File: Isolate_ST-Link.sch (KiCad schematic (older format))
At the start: 17 parts

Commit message: スピードの切り替えにジャンパを追加
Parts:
- added C? (x2): C, symbol C
- added J? (x2): GS3, Connectors:GS3, symbol GS3
- added R?: R, symbol R
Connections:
- net GND: now also J?.3 (G3)
- net GNDPWR: now also C?.1, C?.2, J?.3 (G3)
- net at J?.1 (VBUS): now also U?.1 (V_BUS1), C?.1
- net at U?.12 (PIN): now also R?.2
- net at U?.13 (SPD): now also J?.2 (G2)
- net at U?.14 (VDD2): now also J?.1 (G1), R?.1
- net at U?.3 (VDD1): now also C?.2, J?.1 (G1)
- net at U?.5 (SPU): now also J?.2 (G2)
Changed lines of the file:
@@
 $EndComp
 Wire Wire Line
-	8200 4550 9250 4550
-Wire Wire Line
-	8700 4350 8700 4650
-Wire Wire Line
-	8200 4450 9250 4450
-Wire Wire Line
-	8950 4350 8950 4650
+	8200 4550 8700 4550
+Wire Wire Line
+	8700 4550 9250 4550
+Wire Wire Line
+	8700 4350 8700 4550
+Wire Wire Line
+	8700 4550 8700 4650
+Wire Wire Line
+	8200 4450 8950 4450
+Wire Wire Line
+	8950 4450 9250 4450
+Wire Wire Line
+	8950 4350 8950 4450
+Wire Wire Line
+	8950 4450 8950 4650
 $Comp
 L GND #PWR?
@@
 $EndComp
 Wire Wire Line
-	2000 4650 2000 4850
+	2000 4650 2000 4700
+Wire Wire Line
+	2000 4700 2000 4850
 Wire Wire Line
 	1900 4650 1900 4700
@@
 $EndComp
 Wire Wire Line
-	6900 3200 7100 3200
+	6900 3200 7000 3200
+Wire Wire Line
+	7000 3200 7100 3200
 Wire Wire Line
 	6900 2900 7000 2900
@@
 	5350 3750 5450 3750
 Wire Wire Line
-	5450 3750 5450 4400
+	5450 3750 5450 4350
+Wire Wire Line
+	5450 4350 5450 4400
 Wire Wire Line
 	5350 4350 5450 4350
@@
 $EndComp
 Wire Wire Line
-	4350 4400 4350 3750
+	4350 3750 4350 4350
+Wire Wire Line
+	4350 4350 4350 4400
+Wire Wire Line
+	4000 3750 4350 3750
 Wire Wire Line
 	4350 3750 4450 3750
@@
 Wire Wire Line
 	4150 4350 2300 4350
+$Comp
+L C C?
+U 1 1 59487B46
+P 3800 3800
+F 0 "C?" H 3825 3900 50  0000 L CNN
+F 1 "C" H 3825 3700 50  0000 L CNN
+F 2 "" H 3838 3650 50  0001 C CNN
+F 3 "" H 3800 3800 50  0001 C CNN
+	1    3800 3800
+	1    0    0    -1
+$EndComp
+Wire Wire Line
+	4450 3850 4000 3850
+Wire Wire Line
+	4000 3950 4000 3850
+Wire Wire Line
+	3650 3950 3800 3950
+Wire Wire Line
+	3800 3950 4000 3950
+Wire Wire Line
+	4000 3750 4000 3650
+Wire Wire Line
+	4000 3650 3800 3650
+Connection ~ 4350 3750
+$Comp
+L C C?
+U 1 1 59488111
+P 3800 3500
+F 0 "C?" H 3825 3600 50  0000 L CNN
+F 1 "C" H 3825 3400 50  0000 L CNN
+F 2 "" H 3838 3350 50  0001 C CNN
+F 3 "" H 3800 3500 50  0001 C CNN
+	1    3800 3500
+	1    0    0    -1
+$EndComp
+Wire Wire Line
+	4450 3650 4200 3650
+Wire Wire Line
+	4200 3350 4200 3650
+Wire Wire Line
+	2700 3350 3800 3350
+Wire Wire Line
+	3800 3350 4200 3350
+Wire Wire Line
+	2300 4050 2700 4050
+Wire Wire Line
+	2700 4050 2700 3350
+Connection ~ 3800 3350
+$Comp
+L GS3 J?
+U 1 1 594888C1
+P 3500 4050
+F 0 "J?" H 3550 4250 50  0000 C CNN
+F 1 "GS3" H 3550 3851 50  0000 C CNN
+F 2 "Connectors:GS3" V 3588 3976 50  0001 C CNN
+F 3 "" H 3500 4050 50  0001 C CNN
+	1    3500 4050
+	1    0    0    -1
+$EndComp
+$Comp
+L GS3 J?
+U 1 1 5948896E
+P 6250 3950
+F 0 "J?" H 6300 4150 50  0000 C CNN
+F 1 "GS3" H 6300 3751 50  0000 C CNN
+F 2 "Connectors:GS3" V 6338 3876 50  0001 C CNN
+F 3 "" H 6250 3950 50  0001 C CNN
+	1    6250 3950
+	-1   0    0    -1
+$EndComp
+Wire Wire Line
+	4450 4050 3650 4050
+$Comp
+L GNDPWR #PWR?
+U 1 1 59488AB0
+P 3300 4450
+F 0 "#PWR?" H 3300 4250 50  0001 C CNN
+F 1 "GNDPWR" H 3300 4320 50  0000 C CNN
+F 2 "" H 3300 4400 50  0001 C CNN
+F 3 "" H 3300 4400 50  0001 C CNN
+	1    3300 4450
+	1    0    0    -1
+$EndComp
+Wire Wire Line
+	3350 4150 3300 4150
+Wire Wire Line
+	3300 4150 3300 4450
+Wire Wire Line
+	3350 3950 3300 3950
+Wire Wire Line
+	3300 3950 3300 3750
+Wire Wire Line
+	3300 3750 3650 3750
+Wire Wire Line
+	3650 3750 3650 3950
+Connection ~ 3800 3950
+Wire Wire Line
+	5350 3950 6100 3950
+$Comp
+L GND #PWR?
+U 1 1 5948984E
+P 6400 4400
+F 0 "#PWR?" H 6400 4150 50  0001 C CNN
+F 1 "GND" H 6400 4250 50  0000 C CNN
+F 2 "" H 6400 4400 50  0001 C CNN
+F 3 "" H 6400 4400 50  0001 C CNN
+	1    6400 4400
+	1    0    0    -1
+$EndComp
+Wire Wire Line
+	6400 4400 6400 4050
+Wire Wire Line
+	6400 4050 6400 4050
+Wire Wire Line
+	5350 3850 5950 3850
+Wire Wire Line
+	5950 3850 5950 3850
+Wire Wire Line
+	5950 3850 5950 3700
+Wire Wire Line
+	5950 3700 6400 3700
+Wire Wire Line
+	6400 3700 6400 3850
+Wire Wire Line
+	6400 3850 6400 3850
+$Comp
+L R R?
+U 1 1 59489C26
+P 5700 4050
+F 0 "R?" V 5780 4050 50  0000 C CNN
+F 1 "R" V 5700 4050 50  0000 C CNN
+F 2 "" V 5630 4050 50  0001 C CNN
+F 3 "" H 5700 4050 50  0001 C CNN
+	1    5700 4050
+	0    1    1    0
+$EndComp
+Wire Wire Line
+	5350 4050 5550 4050
+Wire Wire Line
+	5850 4050 5950 4050
+Wire Wire Line
+	5950 4050 5950 3850
+Connection ~ 5950 3850
 $EndSCHEMATC

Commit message: 簡素にした
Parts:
- removed J? (x2): GS3, Connectors:GS3, symbol GS3
- removed R?: R, symbol R
- added C? (x2): C, symbol C
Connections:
- net GND: now also C?.1, C?.2
- net at C?.2, U?.3 (VDD1): now also U?.4 (PDEN), U?.5 (SPU)
- net at U?.14 (VDD2): now also U?.12 (PIN), U?.13 (SPD), C?.2
- net at U?.16 (VBUS2): now also C?.1
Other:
- moved on the sheet: C?
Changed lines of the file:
@@
 $EndComp
 Wire Wire Line
-	8200 4550 8700 4550
-Wire Wire Line
-	8700 4550 9250 4550
-Wire Wire Line
-	8700 4350 8700 4550
-Wire Wire Line
-	8700 4550 8700 4650
-Wire Wire Line
-	8200 4450 8950 4450
-Wire Wire Line
-	8950 4450 9250 4450
-Wire Wire Line
-	8950 4350 8950 4450
-Wire Wire Line
-	8950 4450 8950 4650
+	8200 4550 9250 4550
+Wire Wire Line
+	8700 4350 8700 4650
+Wire Wire Line
+	8200 4450 9250 4450
+Wire Wire Line
+	8950 4350 8950 4650
 $Comp
 L GND #PWR?
@@
 $EndComp
 Wire Wire Line
-	2000 4650 2000 4700
-Wire Wire Line
-	2000 4700 2000 4850
+	2000 4650 2000 4850
 Wire Wire Line
 	1900 4650 1900 4700
@@
 $EndComp
 Wire Wire Line
-	6900 3200 7000 3200
-Wire Wire Line
-	7000 3200 7100 3200
+	6900 3200 7100 3200
 Wire Wire Line
 	6900 2900 7000 2900
@@
 L GND #PWR?
 U 1 1 5949B992
-P 5450 4400
-F 0 "#PWR?" H 5450 4150 50  0001 C CNN
-F 1 "GND" H 5450 4250 50  0000 C CNN
-F 2 "" H 5450 4400 50  0001 C CNN
-F 3 "" H 5450 4400 50  0001 C CNN
-	1    5450 4400
-	1    0    0    -1
-$EndComp
-Wire Wire Line
-	5350 3750 5450 3750
-Wire Wire Line
-	5450 3750 5450 4350
-Wire Wire Line
-	5450 4350 5450 4400
-Wire Wire Line
-	5350 4350 5450 4350
-Connection ~ 5450 4350
+P 5800 4400
+F 0 "#PWR?" H 5800 4150 50  0001 C CNN
+F 1 "GND" H 5800 4250 50  0000 C CNN
+F 2 "" H 5800 4400 50  0001 C CNN
+F 3 "" H 5800 4400 50  0001 C CNN
+	1    5800 4400
+	1    0    0    -1
+$EndComp
+Wire Wire Line
+	5800 3750 5800 4400
+Wire Wire Line
+	5350 4350 6000 4350
+Connection ~ 5800 4350
 $Comp
 L R R?
@@
 L GNDPWR #PWR?
 U 1 1 5949CF3F
-P 4350 4400
-F 0 "#PWR?" H 4350 4200 50  0001 C CNN
-F 1 "GNDPWR" H 4350 4270 50  0000 C CNN
-F 2 "" H 4350 4350 50  0001 C CNN
-F 3 "" H 4350 4350 50  0001 C CNN
-	1    4350 4400
-	1    0    0    -1
-$EndComp
-Wire Wire Line
-	4350 3750 4350 4350
-Wire Wire Line
-	4350 4350 4350 4400
-Wire Wire Line
-	4000 3750 4350 3750
-Wire Wire Line
-	4350 3750 4450 3750
-Wire Wire Line
-	4450 4350 4350 4350
-Connection ~ 4350 4350
+P 4000 4400
+F 0 "#PWR?" H 4000 4200 50  0001 C CNN
+F 1 "GNDPWR" H 4000 4270 50  0000 C CNN
+F 2 "" H 4000 4350 50  0001 C CNN
+F 3 "" H 4000 4350 50  0001 C CNN
+	1    4000 4400
+	1    0    0    -1
+$EndComp
 Wire Wire Line
 	4450 4250 2300 4250
 Wire Wire Line
-	4450 4150 4150 4150
-Wire Wire Line
-	4150 4150 4150 4350
-Wire Wire Line
-	4150 4350 2300 4350
+	4450 4150 3200 4150
+Wire Wire Line
+	3200 4150 3200 4350
+Wire Wire Line
+	3200 4350 2300 4350
 $Comp
 L C C?
 U 1 1 59487B46
-P 3800 3800
-F 0 "C?" H 3825 3900 50  0000 L CNN
-F 1 "C" H 3825 3700 50  0000 L CNN
-F 2 "" H 3838 3650 50  0001 C CNN
-F 3 "" H 3800 3800 50  0001 C CNN
-	1    3800 3800
-	1    0    0    -1
-$EndComp
-Wire Wire Line
-	4450 3850 4000 3850
-Wire Wire Line
-	4000 3950 4000 3850
-Wire Wire Line
-	3650 3950 3800 3950
-Wire Wire Line
-	3800 3950 4000 3950
-Wire Wire Line
-	4000 3750 4000 3650
-Wire Wire Line
-	4000 3650 3800 3650
-Connection ~ 4350 3750
+P 4200 3900
+F 0 "C?" H 4225 4000 50  0000 L CNN
+F 1 "C" H 4225 3800 50  0000 L CNN
+F 2 "" H 4238 3750 50  0001 C CNN
+F 3 "" H 4200 3900 50  0001 C CNN
+	1    4200 3900
+	1    0    0    -1
+$EndComp
+Wire Wire Line
+	4450 3850 4400 3850
+Wire Wire Line
+	4400 3850 4400 4050
+Wire Wire Line
+	4400 3950 4450 3950
 $Comp
 L C C?
 U 1 1 59488111
-P 3800 3500
-F 0 "C?" H 3825 3600 50  0000 L CNN
-F 1 "C" H 3825 3400 50  0000 L CNN
-F 2 "" H 3838 3350 50  0001 C CNN
-F 3 "" H 3800 3500 50  0001 C CNN
-	1    3800 3500
-	1    0    0    -1
-$EndComp
-Wire Wire Line
-	4450 3650 4200 3650
-Wire Wire Line
-	4200 3350 4200 3650
-Wire Wire Line
-	2700 3350 3800 3350
-Wire Wire Line
-	3800 3350 4200 3350
+P 3800 3900
+F 0 "C?" H 3825 4000 50  0000 L CNN
+F 1 "C" H 3825 3800 50  0000 L CNN
+F 2 "" H 3838 3750 50  0001 C CNN
+F 3 "" H 3800 3900 50  0001 C CNN
+	1    3800 3900
+	1    0    0    -1
+$EndComp
+Wire Wire Line
+	2700 3650 4450 3650
 Wire Wire Line
 	2300 4050 2700 4050
 Wire Wire Line
-	2700 4050 2700 3350
-Connection ~ 3800 3350
-$Comp
-L GS3 J?
-U 1 1 594888C1
-P 3500 4050
-F 0 "J?" H 3550 4250 50  0000 C CNN
-F 1 "GS3" H 3550 3851 50  0000 C CNN
-F 2 "Connectors:GS3" V 3588 3976 50  0001 C CNN
-F 3 "" H 3500 4050 50  0001 C CNN
-	1    3500 4050
-	1    0    0    -1
-$EndComp
-$Comp
-L GS3 J?
-U 1 1 5948896E
-P 6250 3950
-F 0 "J?" H 6300 4150 50  0000 C CNN
-F 1 "GS3" H 6300 3751 50  0000 C CNN
-F 2 "Connectors:GS3" V 6338 3876 50  0001 C CNN
-F 3 "" H 6250 3950 50  0001 C CNN
-	1    6250 3950
-	-1   0    0    -1
-$EndComp
-Wire Wire Line
-	4450 4050 3650 4050
-$Comp
-L GNDPWR #PWR?
-U 1 1 59488AB0
-P 3300 4450
-F 0 "#PWR?" H 3300 4250 50  0001 C CNN
-F 1 "GNDPWR" H 3300 4320 50  0000 C CNN
-F 2 "" H 3300 4400 50  0001 C CNN
-F 3 "" H 3300 4400 50  0001 C CNN
-	1    3300 4450
-	1    0    0    -1
-$EndComp
-Wire Wire Line
-	3350 4150 3300 4150
-Wire Wire Line
-	3300 4150 3300 4450
-Wire Wire Line
-	3350 3950 3300 3950
-Wire Wire Line
-	3300 3950 3300 3750
-Wire Wire Line
-	3300 3750 3650 3750
-Wire Wire Line
-	3650 3750 3650 3950
-Connection ~ 3800 3950
-Wire Wire Line
-	5350 3950 6100 3950
-$Comp
-L GND #PWR?
-U 1 1 5948984E
-P 6400 4400
-F 0 "#PWR?" H 6400 4150 50  0001 C CNN
-F 1 "GND" H 6400 4250 50  0000 C CNN
-F 2 "" H 6400 4400 50  0001 C CNN
-F 3 "" H 6400 4400 50  0001 C CNN
-	1    6400 4400
-	1    0    0    -1
-$EndComp
-Wire Wire Line
-	6400 4400 6400 4050
-Wire Wire Line
-	6400 4050 6400 4050
-Wire Wire Line
-	5350 3850 5950 3850
-Wire Wire Line
-	5950 3850 5950 3850
-Wire Wire Line
-	5950 3850 5950 3700
-Wire Wire Line
-	5950 3700 6400 3700
-Wire Wire Line
-	6400 3700 6400 3850
-Wire Wire Line
-	6400 3850 6400 3850
-$Comp
-L R R?
-U 1 1 59489C26
-P 5700 4050
-F 0 "R?" V 5780 4050 50  0000 C CNN
-F 1 "R" V 5700 4050 50  0000 C CNN
-F 2 "" V 5630 4050 50  0001 C CNN
-F 3 "" H 5700 4050 50  0001 C CNN
-	1    5700 4050
-	0    1    1    0
-$EndComp
-Wire Wire Line
-	5350 4050 5550 4050
-Wire Wire Line
-	5850 4050 5950 4050
-Wire Wire Line
-	5950 4050 5950 3850
-Connection ~ 5950 3850
+	5350 4050 5600 4050
+Connection ~ 4400 3950
+Wire Wire Line
+	4200 4050 4450 4050
+Connection ~ 4400 4050
+Wire Wire Line
+	4000 3750 4450 3750
+Connection ~ 4200 3750
+Wire Wire Line
+	4000 3750 4000 4400
+Wire Wire Line
+	3800 4350 4450 4350
+Connection ~ 4000 4350
+$Comp
+L C C?
+U 1 1 5949101E
+P 5600 3900
+F 0 "C?" H 5625 4000 50  0000 L CNN
+F 1 "C" H 5625 3800 50  0000 L CNN
+F 2 "" H 5638 3750 50  0001 C CNN
+F 3 "" H 5600 3900 50  0001 C CNN
+	1    5600 3900
+	1    0    0    -1
+$EndComp
+Wire Wire Line
+	5350 3850 5400 3850
+Wire Wire Line
+	5400 3850 5400 4050
+Connection ~ 5400 4050
+Wire Wire Line
+	5350 3950 5400 3950
+Connection ~ 5400 3950
+Wire Wire Line
+	5350 3650 6000 3650
+Wire Wire Line
+	5350 3750 5800 3750
+Connection ~ 5600 3750
+$Comp
+L C C?
+U 1 1 59497D6D
+P 6000 3900
+F 0 "C?" H 6025 4000 50  0000 L CNN
+F 1 "C" H 6025 3800 50  0000 L CNN
+F 2 "" H 6038 3750 50  0001 C CNN
+F 3 "" H 6000 3900 50  0001 C CNN
+	1    6000 3900
+	1    0    0    -1
+$EndComp
+Wire Wire Line
+	6000 3650 6000 3750
+Wire Wire Line
+	6000 4350 6000 4050
+Wire Wire Line
+	2700 4050 2700 3650
+Wire Wire Line
+	3800 4350 3800 4050
+Wire Wire Line
+	3800 3750 3800 3650
+Connection ~ 3800 3650
 $EndSCHEMATC

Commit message: 基板起こした
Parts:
- removed C? (x3): C, symbol C
- removed R? (x2): R, symbol R
- added C1: 47u, Capacitors_SMD:C_1206, symbol C
- added C2, C3, C5: 0.1u, Capacitors_SMD:C_0603, symbol C
- added C6, C7: 1u, Capacitors_SMD:C_0603, symbol C
- added D10, D9: D, Diodes_SMD:D_SOD-123F, symbol D
- added D5, D6, D7, D8: LED, LEDs:LED_0603, symbol LED
- added F1, F2: Fuse, Capacitors_SMD:C_0603, symbol Fuse
- added J4, J5: CONN_01X02, Connectors_JST:JST_EH_S02B-EH_02x2.50mm_Angled, symbol CONN_01X02
- added L1: L, Capacitors_SMD:C_0603, symbol L
- added Q1: BSS138, TO_SOT_Packages_SMD:SOT-23, symbol BSS138
- added R1: 100k, Resistors_SMD:R_0603, symbol R
- added R10, R2, R3: 24, Resistors_SMD:R_0603, symbol R
- added R13, R17, R18, R19, R20: 1k, Resistors_SMD:R_0603, symbol R
- added R4: 1.5k, Resistors_SMD:R_0603, symbol R
- added R5: 10k, Resistors_SMD:R_0603, symbol R
- added R6: 36k, Resistors_SMD:R_0603, symbol R
- added R7: 100, Resistors_SMD:R_0603, symbol R
- added U1: MAU10x, Converters_DCDC_ACDC:DCDC-Conv_Minimax_MAU10x, symbol MAU10x
- added U3: APE8865NR-33-HF-3, TO_SOT_Packages_SMD:SOT-23, symbol APE8865NR-33-HF-3
- C4: renamed from C?; value C -> 0.1u; footprint (none) -> Capacitors_SMD:C_0603
- D1, D2: renamed from D?; footprint (none) -> LEDs:LED_0603
- D3, D4: renamed from D?; footprint (none) -> Diodes_SMD:D_SOD-323_HandSoldering
- J1: renamed from J?; footprint (none) -> Connect:USB_Micro-B
- J2: renamed from J?; footprint (none) -> Connectors_JST:JST_EH_S06B-EH_06x2.50mm_Angled
- J3: renamed from J?; footprint (none) -> Connectors_JST:JST_EH_S04B-EH_04x2.50mm_Angled
- R11: renamed from R?; value R -> 24; footprint (none) -> Resistors_SMD:R_0603
- R12: renamed from R?; value R -> 1k; footprint (none) -> Resistors_SMD:R_0603
- R14, R15, R16, R8, R9: renamed from R?; footprint (none) -> Resistors_SMD:R_0603
- U2: renamed from U?; footprint (none) -> Housings_SOIC:SOIC-16W_7.5x10.3mm_Pitch1.27mm
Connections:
- net +3V3: now also C7.1, D10.2 (A), D6.2 (A), D7.2 (A), D8.2 (A), Q1.3 (D), R13.1, U3.2 (VOUT)
- net GND: now also C5.2, C6.2, C7.2, J4.2 (P2), J5.2 (P2), R17.1, R18.1, R6.1, U1.4 (-Vout), U3.3 (GND)
- net GNDPWR: now also C1.2, C2.2, C3.1, R1.2, U1.2 (-Vin)
- net MCU/UART_RX: now also R19.1
- net MCU/UART_TX: now also R13.2, R20.1
- net MCU/USB_DM: now also R10.2
- net MCU/USB_RENUMn: now also R7.2
- net at J1.1 (VBUS): now also F1.2, F2.2; no longer U2.1 (V_BUS1)
- net at J1.2 (D-): now also R3.2; no longer U2.6 (UD-)
- net at J1.3 (D+): now also R2.1; no longer U2.7 (UD+)
- net at J1.4 (ID): now also R1.1
- net at U2.3 (VDD1), U2.4 (PDEN), U2.5 (SPU): now also C3.2
- net +5V: now reaches U2.16 (VBUS2)
- net +5V: now also C5.1, C6.1, D5.2 (A), D9.2 (A), R5.2, U1.6 (+Vout), U3.1 (VIN)
- net at R11.2, U2.10 (DD+): now also R4.2
- net at U2.11 (DD-): now also R10.1
- new net: R3.1, U2.6 (UD-)
- new net: R2.2, U2.7 (UD+)
- new net: F1.1, F2.1, L1.1
- new net: D8.1 (K), R20.2
- new net: D7.1 (K), R19.2
- new net: D10.1 (K), J5.1 (P1)
- new net: D9.1 (K), J4.1 (P1)
- new net: D6.1 (K), R18.2
- new net: D5.1 (K), R17.2
- new net: Q1.1 (G), R5.1, R6.2, R7.1
- new net: Q1.2 (S), R4.1
- new net +5VP: C1.1, C2.1, L1.2, U1.1 (+Vin), U2.1 (V_BUS1)
- no-connect marks 0 -> 1
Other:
- moved on the sheet: C4, D1, D2, D3, D4, J1, J2, J3, R11, R12, R14, R15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

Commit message: microUSBの参照元を変更
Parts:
- J1: footprint Connect:USB_Micro-B -> Connectors:USB_Micro-B
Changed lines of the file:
@@
 F 0 "J1" H 600 4700 50  0000 L CNN
 F 1 "USB_OTG" H 600 4600 50  0000 L CNN
-F 2 "Connect:USB_Micro-B" H 950 4200 50  0001 C CNN
+F 2 "Connectors:USB_Micro-B" H 950 4200 50  0001 C CNN
 F 3 "" H 950 4200 50  0001 C CNN
 	1    800  4250

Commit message: ツェナーダイオードの参照元を変更
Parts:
- D3, D4: footprint Diodes_SMD:D_SOD-323_HandSoldering -> Diodes_SMD:D_SOD-323
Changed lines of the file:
@@
 F 0 "D3" H 7950 4790 50  0000 C CNN
 F 1 "D_Zener_Small" H 7950 4610 50  0000 C CNN
-F 2 "Diodes_SMD:D_SOD-323_HandSoldering" V 7950 4700 50  0001 C CNN
+F 2 "Diodes_SMD:D_SOD-323" V 7950 4700 50  0001 C CNN
 F 3 "" V 7950 4700 50  0001 C CNN
 	1    7950 4700
@@
 F 0 "D4" H 8200 4790 50  0000 C CNN
 F 1 "D_Zener_Small" H 8200 4610 50  0000 C CNN
-F 2 "Diodes_SMD:D_SOD-323_HandSoldering" V 8200 4700 50  0001 C CNN
+F 2 "Diodes_SMD:D_SOD-323" V 8200 4700 50  0001 C CNN
 F 3 "" V 8200 4700 50  0001 C CNN
 	1    8200 4700

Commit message: 完成したのでしばらく寝かせる
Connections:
- net MCU/UART_RX: now also D4.1 (K), J3.2 (P2), R13.2, R20.1; no longer D3.1 (K), J3.3 (P3), R12.2, R19.1
- net MCU/UART_TX: now also D3.1 (K), J3.3 (P3), R12.2, R19.1; no longer D4.1 (K), J3.2 (P2), R13.2, R20.1
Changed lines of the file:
@@
 F0 "MCU" 60
 F1 "MCU.sch" 60
-F2 "UART_TX" O R 7450 4450 60
-F3 "UART_RX" I R 7450 4550 60
+F2 "UART_TX" O R 7450 4550 60
+F3 "UART_RX" I R 7450 4450 60
 F4 "LED_STLINK" O L 6350 3200 60
 F5 "USB_DM" I L 6350 4150 60

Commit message: ダンピング抵抗追加 分圧抵抗に変更
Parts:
- added R?: 22, Resistors_SMD:R_0603, symbol R
- U3: symbol APE8865NR-33-HF-3 -> APE8865NR-33-HF-3-RESCUE-Isolate_ST-Link
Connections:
- net T_JTCK: now also R?.2; no longer J2.2 (P2)
- new net: J2.2 (P2), R?.1
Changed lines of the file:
@@
 EESchema Schematic File Version 2
+LIBS:Isolate_ST-Link-rescue
 LIBS:power
 LIBS:device
@@
 	0    1    1    0
 $EndComp
-Wire Wire Line
-	7950 3300 8500 3300
 $Comp
 L R R9
@@
 	1900 3650 2900 3650
 $Comp
-L APE8865NR-33-HF-3 U3
+L APE8865NR-33-HF-3-RESCUE-Isolate_ST-Link U3
 U 1 1 594BC3C2
 P 7200 2300
@@
 	1150 3850 1150 4050
 Connection ~ 1150 4050
+$Comp
+L R R?
+U 1 1 59CA9CFA
+P 8300 3300
+F 0 "R?" V 8380 3300 50  0000 C CNN
+F 1 "22" V 8300 3300 50  0000 C CNN
+F 2 "Resistors_SMD:R_0603" V 8230 3300 50  0001 C CNN
+F 3 "" H 8300 3300 50  0001 C CNN
+	1    8300 3300
+	0    1    1    0
+$EndComp
+Wire Wire Line
+	8450 3300 8500 3300
+Wire Wire Line
+	8150 3300 7950 3300
 $EndSCHEMATC

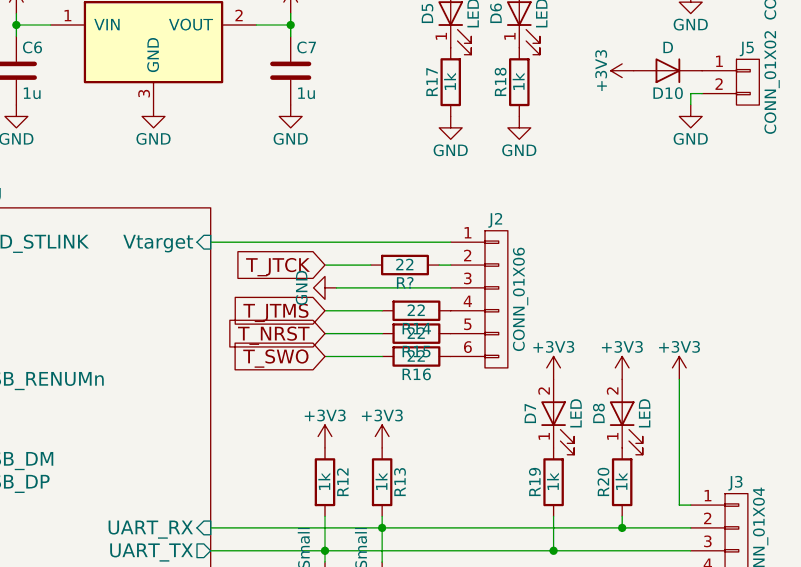
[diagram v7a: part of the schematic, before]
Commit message: 部品割当して基板の修正
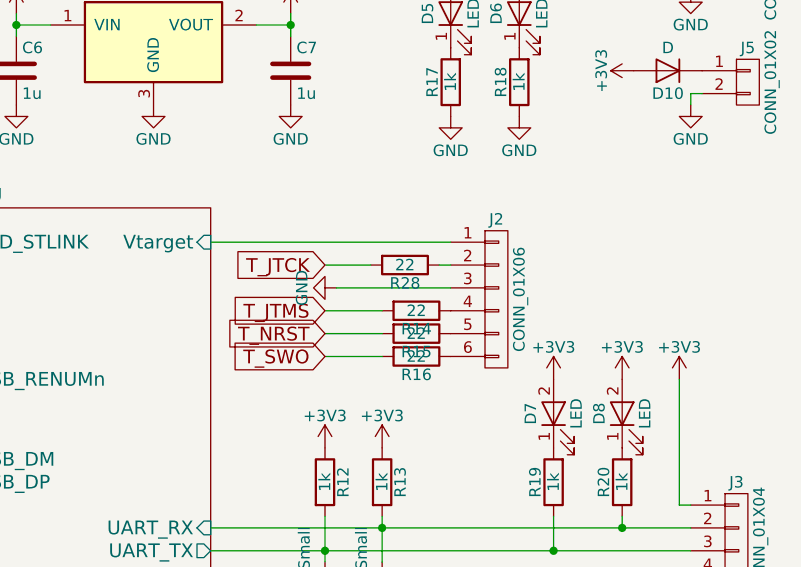
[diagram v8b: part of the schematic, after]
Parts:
- gave numbers to parts that had none: 1
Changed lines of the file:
@@
 Connection ~ 1150 4050
 $Comp
-L R R?
+L R R28
 U 1 1 59CA9CFA
 P 8300 3300
-F 0 "R?" V 8380 3300 50  0000 C CNN
+F 0 "R28" V 8380 3300 50  0000 C CNN
 F 1 "22" V 8300 3300 50  0000 C CNN
 F 2 "Resistors_SMD:R_0603" V 8230 3300 50  0001 C CNN
